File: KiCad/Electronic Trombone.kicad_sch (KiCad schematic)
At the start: 14 parts, among them J1 691137710004, U1 TL074, U2 TL074, U9 CD74HC4051E

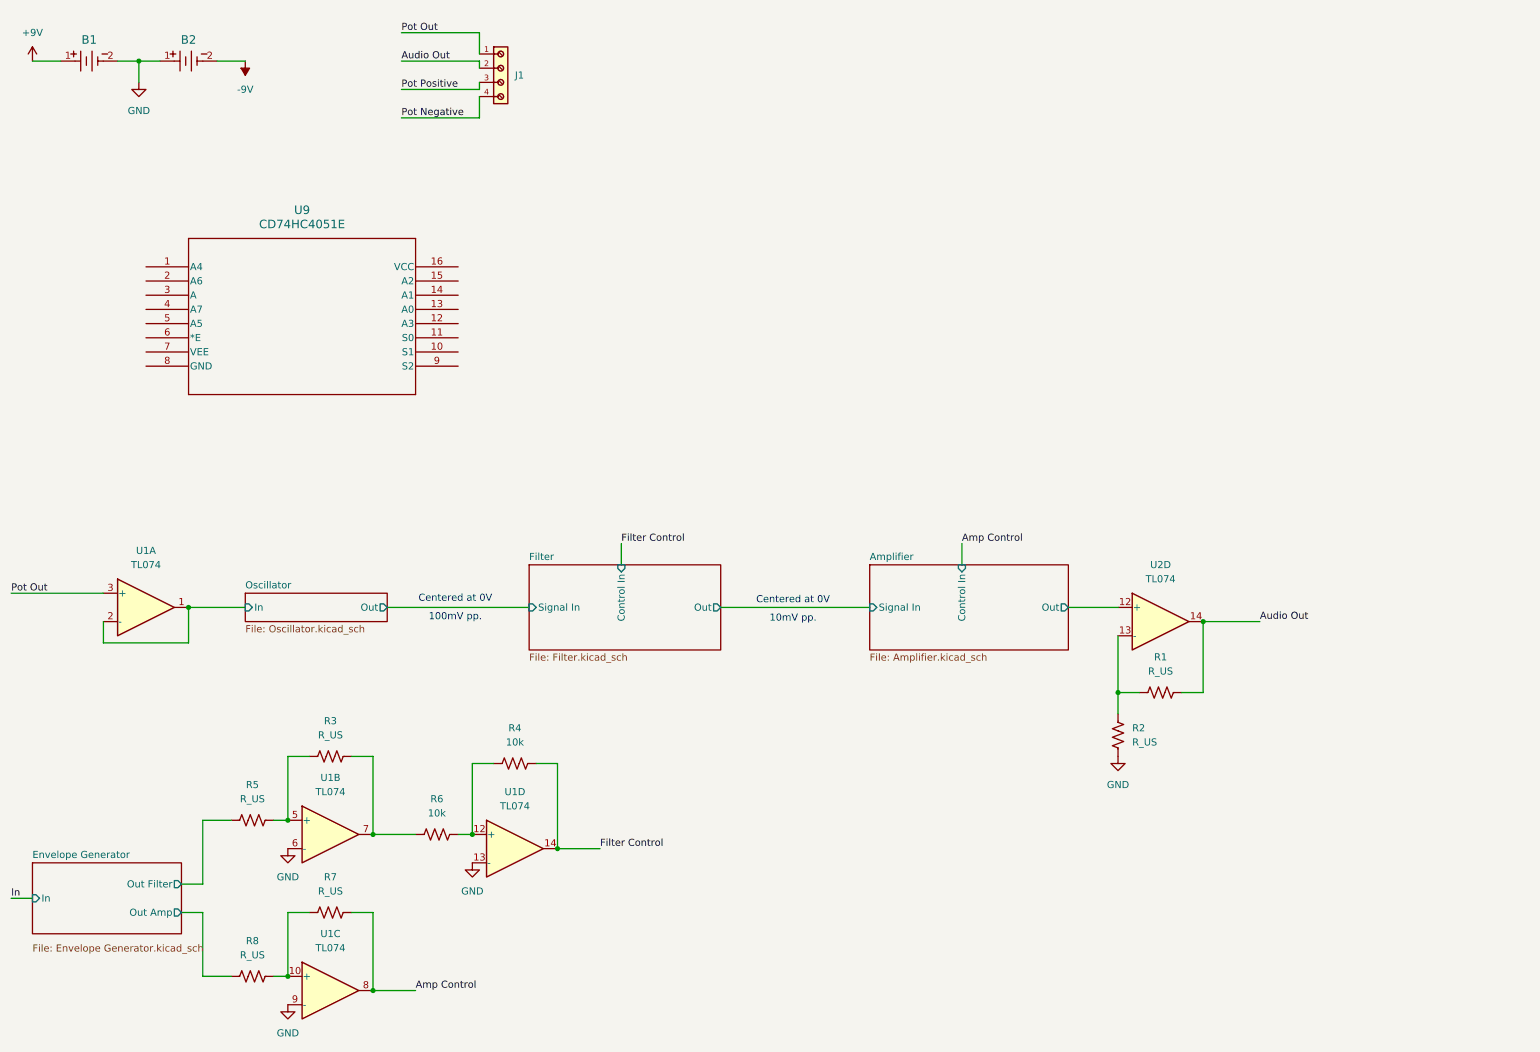
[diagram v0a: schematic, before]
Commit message: added potentiometer voltage control cct
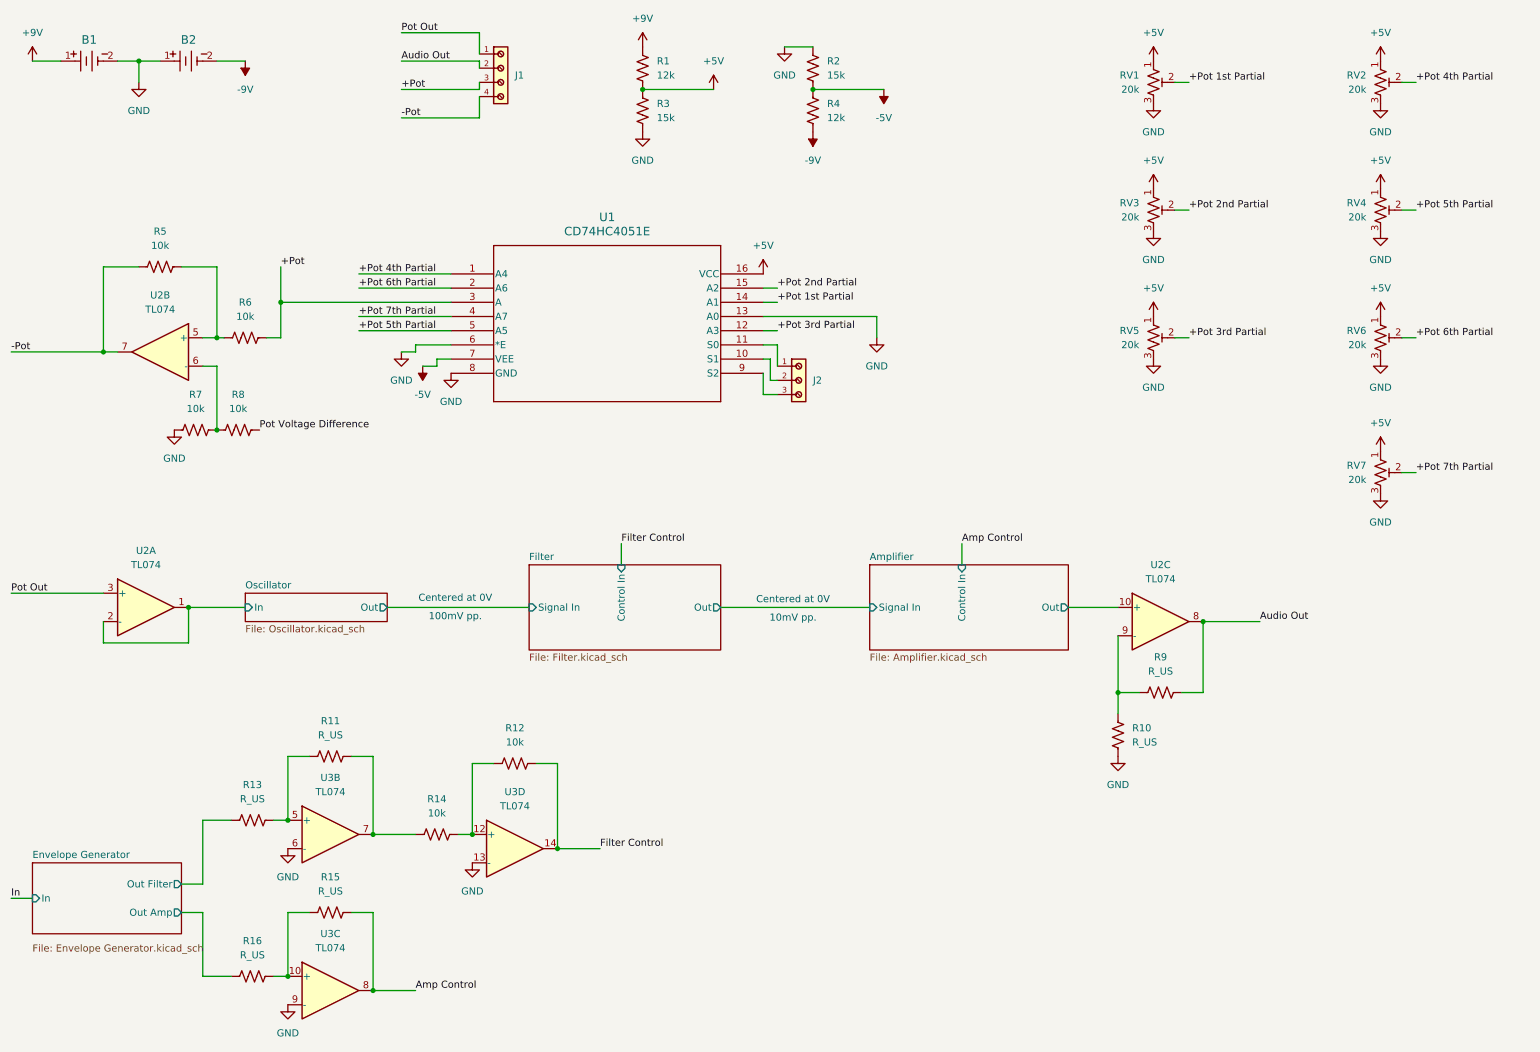
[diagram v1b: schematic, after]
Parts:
- added J2: 691137710003, Header 691137710003:691137710003, symbol Header 691137710003:691137710003
- added R1, R4: 12k, Resistor_SMD:R_0201_0603Metric, symbol Device:R_US
- added R2, R3: 15k, Resistor_SMD:R_0201_0603Metric, symbol Device:R_US
- added R5, R6, R7, R8: 10k, Resistor_SMD:R_0201_0603Metric, symbol Device:R_US
- added RV1, RV2, RV3, RV4, RV5, RV6, RV7: 20k, Potentiometer_SMD:Potentiometer_Bourns_TC33X_Vertical, symbol Device:R_Potentiometer_Trim_US
- added unit 2 of U2
- renumbered R2 to R10, R3 to R11, R4 to R12, R5 to R13, R6 to R14, R7 to R15, R8 to R16, R1 to R9, U9 to U1, U1 to U2, U1 to U3
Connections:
- net Pot Positive is gone; now on net +Pot: J1.3
- net +9V: now also R1.2
- net -9V: now also R4.1
- net Amplifier/Out: now also U2.10 (+); no longer U2.12 (+)
- net Audio Out: now also U2.8; no longer U2.14
- net GND: now also U1.13 (A0), U1.6 (*E), U1.8 (GND), R2.2, R3.1, R7.1, RV1.3, RV2.3, RV3.3, RV4.3, RV5.3, RV6.3, RV7.3
- net at R10.2, R9.1: now also U2.9 (-); no longer U2.13 (-)
- net +Pot 4th Partial: now reaches U1.1 (A4)
- net +Pot 4th Partial: now also RV2.2
- net at U1.10 (S1): now also J2.2
- net at U1.11 (S0): now also J2.1
- net +Pot 3rd Partial: now reaches U1.12 (A3)
- net +Pot 3rd Partial: now also RV5.2
- net +Pot 1st Partial: now reaches U1.14 (A1)
- net +Pot 1st Partial: now also RV1.2
- net +Pot 2nd Partial: now reaches U1.15 (A2)
- net +Pot 2nd Partial: now also RV3.2
- net +5V: now reaches U1.16 (VCC)
- net +5V: now also R1.1, R3.2, RV1.1, RV2.1, RV3.1, RV4.1, RV5.1, RV6.1, RV7.1
- net +Pot 6th Partial: now reaches U1.2 (A6)
- net +Pot 6th Partial: now also RV6.2
- net +Pot: now reaches U1.3 (A)
- net +Pot: now also R6.2
- net +Pot 7th Partial: now reaches U1.4 (A7)
- net +Pot 7th Partial: now also RV7.2
- net +Pot 5th Partial: now reaches U1.5 (A5)
- net +Pot 5th Partial: now also RV4.2
- net -5V: now reaches U1.7 (VEE)
- net -5V: now also R2.1, R4.2
- net at U1.9 (S2): now also J2.3
- net Pot Negative renamed -Pot
- net -Pot: now also R5.1, U2.7
- new net: R5.2, R6.1, U2.5 (+)
- new net: R7.2, R8.1, U2.6 (-)
- new net Pot Voltage Difference: R8.2
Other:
- moved on the sheet: U1

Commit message: added volume control knob
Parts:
- added RV8: 100k, Potentiometer 51CAD_E24_A20L:POT_51CAD_12P5X13P25_BRN, symbol Device:R_Potentiometer_US
- added unit 4 of U2
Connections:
- net Audio Out: now also U2.13 (-), U2.14; no longer R9.2, U2.8
- net GND: now also RV8.3
- new net: RV8.2, U2.12 (+)
- new net: R9.2, RV8.1, U2.8

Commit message: added power switch, decoupling caps, and unused IC pins
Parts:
- removed B1, B2: BC9VPC, Battery Holder BC9VPC:BC9VPC_MPD, symbol 2026-06-10_00-17-41:BC9VPC
- removed R1, R4: 12k, Resistor_SMD:R_0201_0603Metric, symbol Device:R_US
- removed R2, R3: 15k, Resistor_SMD:R_0201_0603Metric, symbol Device:R_US
- RV8: footprint Potentiometer 51CAD_E24_A20L:POT_51CAD_12P5X13P25_BRN -> Potentiometer 100k PTV09A-2020F-B104:Potentiometer 100k PTV09A-2020F-B104
- renumbered R5 to R1, R14 to R10, R15 to R11, R16 to R12, R6 to R2, R7 to R3, R8 to R4, R9 to R5, R10 to R6, R11 to R7, R12 to R8, R13 to R9
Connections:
- net Amp Control: now also U3.7; no longer U3.8
- net Filter Control: now also U3.8; no longer U3.14
- net GND: now also U3.2 (-), U3.6 (-), U3.9 (-); no longer U3.13 (-), U3.6 (-), U3.9 (-)
- net at R10.2, R8.1: now also U3.10 (+); no longer U3.12 (+)
- net at R7.1, R9.2: now also U3.3 (+); no longer U3.5 (+)
- net at R10.1, R7.2: now also U3.1; no longer U3.7
- net at R11.1, R12.2: now also U3.5 (+); no longer U3.10 (+)
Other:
- moved on the sheet: J1
